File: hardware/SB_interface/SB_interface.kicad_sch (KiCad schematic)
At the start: 7 parts, among them J1 8P8C, J2 8P8C, J3 8P8C, K1 J104D2C12VDC.36S, Q1 2N7002

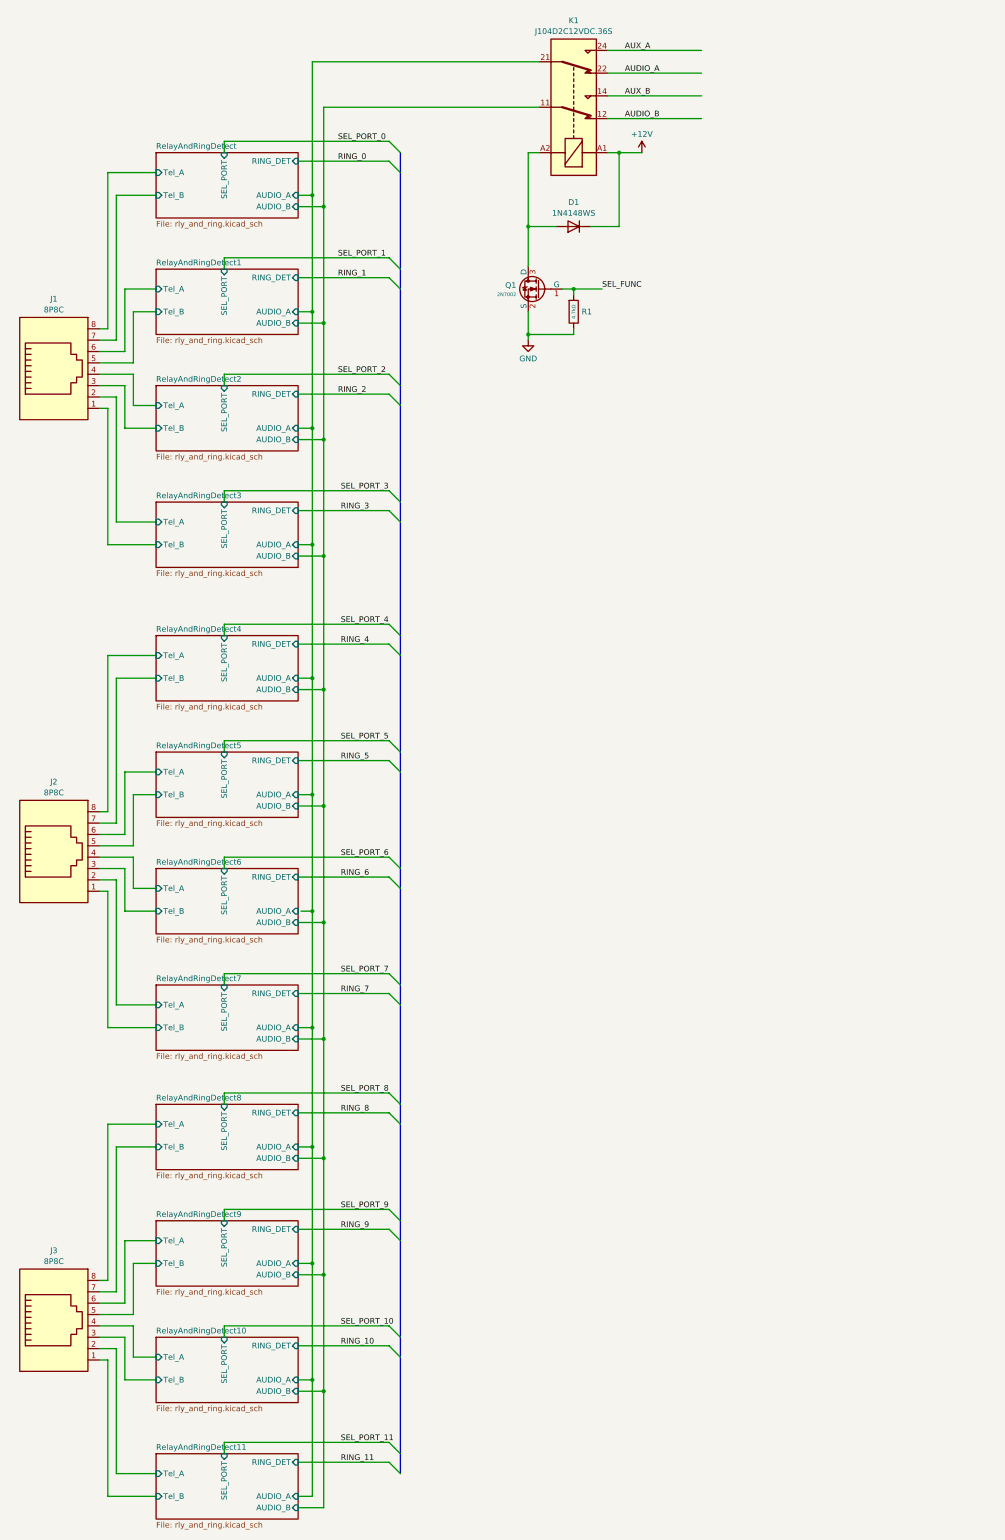
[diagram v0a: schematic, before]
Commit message: current source for ring det. + main 8p8c pinout corrected
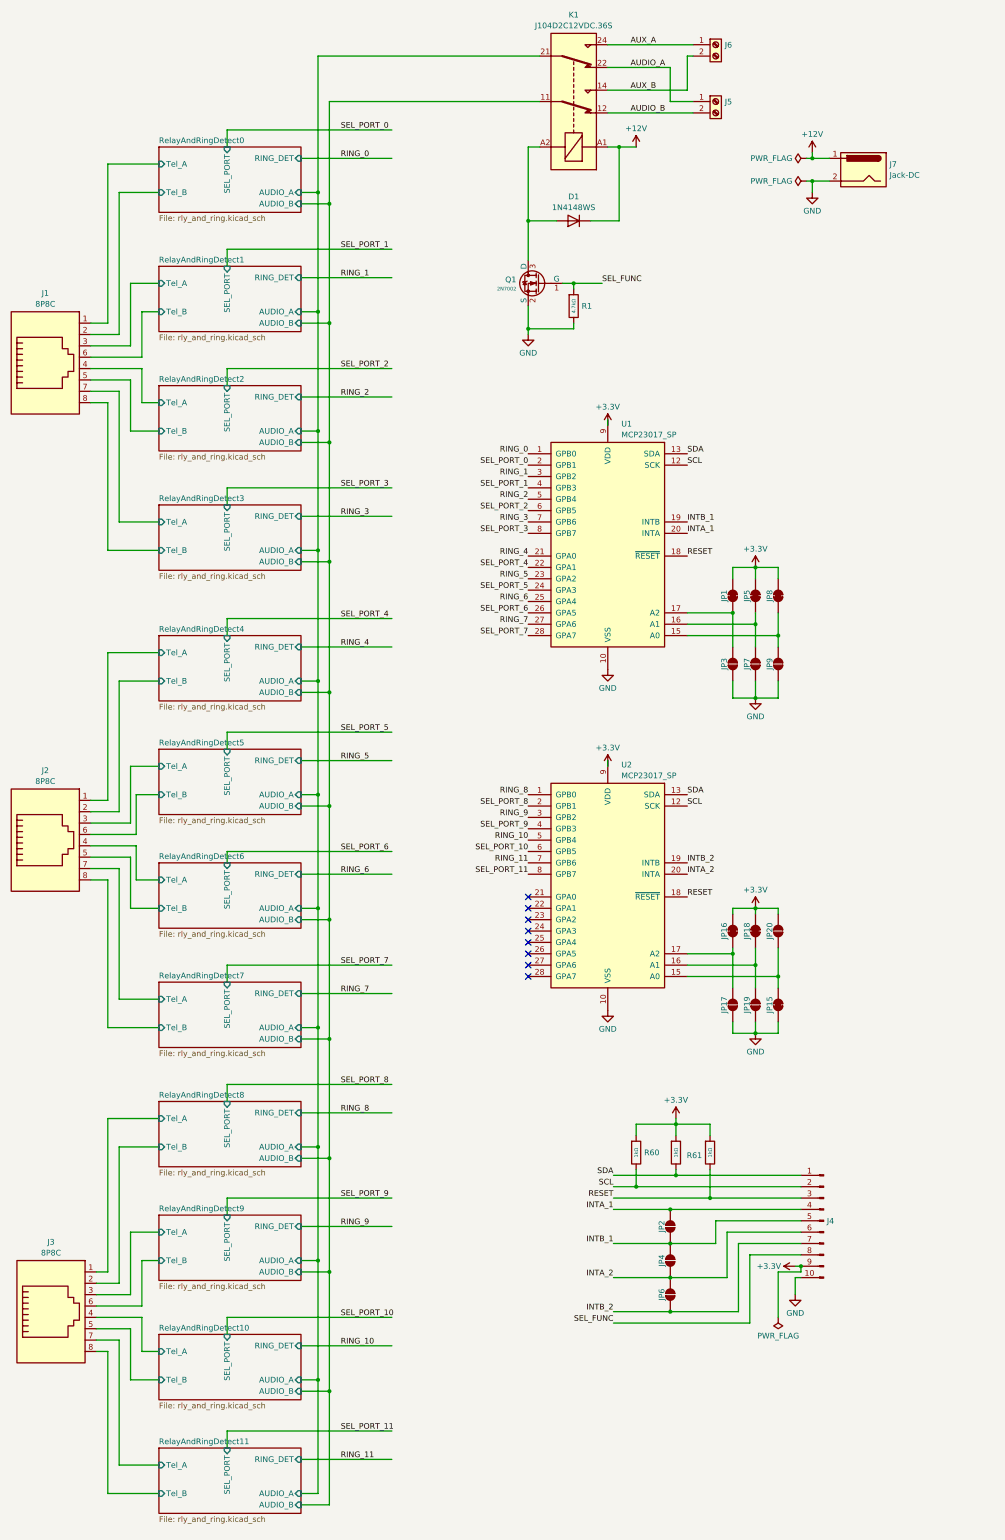
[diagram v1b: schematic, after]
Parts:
- added J4: Conn_01x10_Pin, symbol Connector:Conn_01x10_Pin
- added J5, J6: Screw_Terminal_01x02, symbol Connector:Screw_Terminal_01x02
- added J7: Jack-DC, symbol Connector:Jack-DC
- added JP1, JP15, JP16, JP18, JP5, JP8: SolderJumper_2_Bridged, symbol Jumper:SolderJumper_2_Bridged
- added JP17, JP19, JP2, JP20, JP3, JP4, JP6, JP7, JP9: SolderJumper_2_Open, symbol Jumper:SolderJumper_2_Open
- added R60, R61, R62: 1kΩ, PCM_JLCPCB:R_0805, symbol PCM_JLCPCB-Resistors:0805,1kΩ
- added U1, U2: MCP23017_SP, Package_DIP:DIP-28_W7.62mm, symbol Interface_Expansion:MCP23017_SP
- J1, J2, J3: symbol Connector:8P8C -> sb_interface:8P8C_TelPairs
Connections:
- net RelayAndRingDetect/Tel_A is gone; now on net RelayAndRingDetect3/Tel_B: J1.8
- net RelayAndRingDetect/Tel_B is gone; now on net RelayAndRingDetect3/Tel_A: J1.7
- net +12V: now also J7.1
- net AUDIO_A: now also J5.1 (Pin_1)
- net AUDIO_B: now also J5.2 (Pin_2)
- net AUX_A: now also J6.1 (Pin_1)
- net AUX_B: now also J6.2 (Pin_2)
- net GND: now also J4.10 (Pin_10), J7.2, JP15.2 (B), JP17.1 (A), JP19.1 (A), JP3.1 (A), JP7.1 (A), JP9.1 (A), U1.10 (VSS), U2.10 (VSS)
- net RING_0: now also U1.1 (GPB0)
- net RING_1: now also U1.3 (GPB2)
- net RING_10: now also U2.5 (GPB4)
- net RING_11: now also U2.7 (GPB6)
- net RING_2: now also U1.5 (GPB4)
- net RING_3: now also U1.7 (GPB6)
- net RING_4: now also U1.21 (GPA0)
- net RING_5: now also U1.23 (GPA2)
- net RING_6: now also U1.25 (GPA4)
- net RING_7: now also U1.27 (GPA6)
- net RING_8: now also U2.1 (GPB0)
- net RING_9: now also U2.3 (GPB2)
- net RelayAndRingDetect1/Tel_A: now also J1.3; no longer J1.6
- net RelayAndRingDetect1/Tel_B: now also J1.6; no longer J1.5
- net RelayAndRingDetect10/Tel_B: now also J3.5; no longer J3.3
- net RelayAndRingDetect11/Tel_A: now also J3.7; no longer J3.2
- net RelayAndRingDetect11/Tel_B: now also J3.8; no longer J3.1
- net RelayAndRingDetect2/Tel_B: now also J1.5; no longer J1.3
- net RelayAndRingDetect3/Tel_A: no longer J1.2
- net RelayAndRingDetect3/Tel_B: no longer J1.1
- net RelayAndRingDetect4/Tel_A: now also J2.1; no longer J2.8
- net RelayAndRingDetect4/Tel_B: now also J2.2; no longer J2.7
- net RelayAndRingDetect5/Tel_A: now also J2.3; no longer J2.6
- net RelayAndRingDetect5/Tel_B: now also J2.6; no longer J2.5
- net RelayAndRingDetect6/Tel_B: now also J2.5; no longer J2.3
- net RelayAndRingDetect7/Tel_A: now also J2.7; no longer J2.2
- net RelayAndRingDetect7/Tel_B: now also J2.8; no longer J2.1
- net RelayAndRingDetect8/Tel_A: now also J3.1; no longer J3.8
- net RelayAndRingDetect8/Tel_B: now also J3.2; no longer J3.7
- net RelayAndRingDetect9/Tel_A: now also J3.3; no longer J3.6
- net RelayAndRingDetect9/Tel_B: now also J3.6; no longer J3.5
- net SEL_FUNC: now also J4.8 (Pin_8)
- net SEL_PORT_0: now also U1.2 (GPB1)
- net SEL_PORT_1: now also U1.4 (GPB3)
- net SEL_PORT_10: now also U2.6 (GPB5)
- net SEL_PORT_11: now also U2.8 (GPB7)
- net SEL_PORT_2: now also U1.6 (GPB5)
- net SEL_PORT_3: now also U1.8 (GPB7)
- net SEL_PORT_4: now also U1.22 (GPA1)
- net SEL_PORT_5: now also U1.24 (GPA3)
- net SEL_PORT_6: now also U1.26 (GPA5)
- net SEL_PORT_7: now also U1.28 (GPA7)
- net SEL_PORT_8: now also U2.2 (GPB1)
- net SEL_PORT_9: now also U2.4 (GPB3)
- net RelayAndRingDetect/AUDIO_A renamed RelayAndRingDetect0/AUDIO_A
- net RelayAndRingDetect/AUDIO_B renamed RelayAndRingDetect0/AUDIO_B
- new net: JP16.2 (B), JP17.2 (B), U2.17 (A2)
- new net: JP15.1 (A), JP20.1 (A), U2.15 (A0)
- new net: JP1.2 (B), JP3.2 (B), U1.17 (A2)
- new net: JP18.2 (B), JP19.2 (B), U2.16 (A1)
- new net: JP5.2 (B), JP7.2 (B), U1.16 (A1)
- new net: JP8.2 (B), JP9.2 (B), U1.15 (A0)
- new net +3.3V: J4.9 (Pin_9), JP1.1 (A), JP16.1 (A), JP18.1 (A), JP20.2 (B), JP5.1 (A), JP8.1 (A), R60.1, R61.1, R62.1, U1.9 (VDD), U2.9 (VDD)
- new net INTA_1: J4.4 (Pin_4), JP2.2 (B), U1.20 (INTA)
- new net INTA_2: J4.6 (Pin_6), JP4.1 (A), JP6.2 (B), U2.20 (INTA)
- new net INTB_1: J4.5 (Pin_5), JP2.1 (A), JP4.2 (B), U1.19 (INTB)
- new net INTB_2: J4.7 (Pin_7), JP6.1 (A), U2.19 (INTB)
- new net RESET: J4.3 (Pin_3), R62.2, U1.18 (~{RESET}), U2.18 (~{RESET})
- new net RelayAndRingDetect0/Tel_A: J1.1
- new net RelayAndRingDetect0/Tel_B: J1.2
- new net SCL: J4.2 (Pin_2), R60.2, U1.12 (SCK), U2.12 (SCK)
- new net SDA: J4.1 (Pin_1), R61.2, U1.13 (SDA), U2.13 (SDA)
- no-connect marks 0 -> 8
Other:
- removed sheet RelayAndRingDetect
- added sheet RelayAndRingDetect0 (rly_and_ring.kicad_sch)
- moved on the sheet: D1, J1, J2, J3, K1, Q1, R1

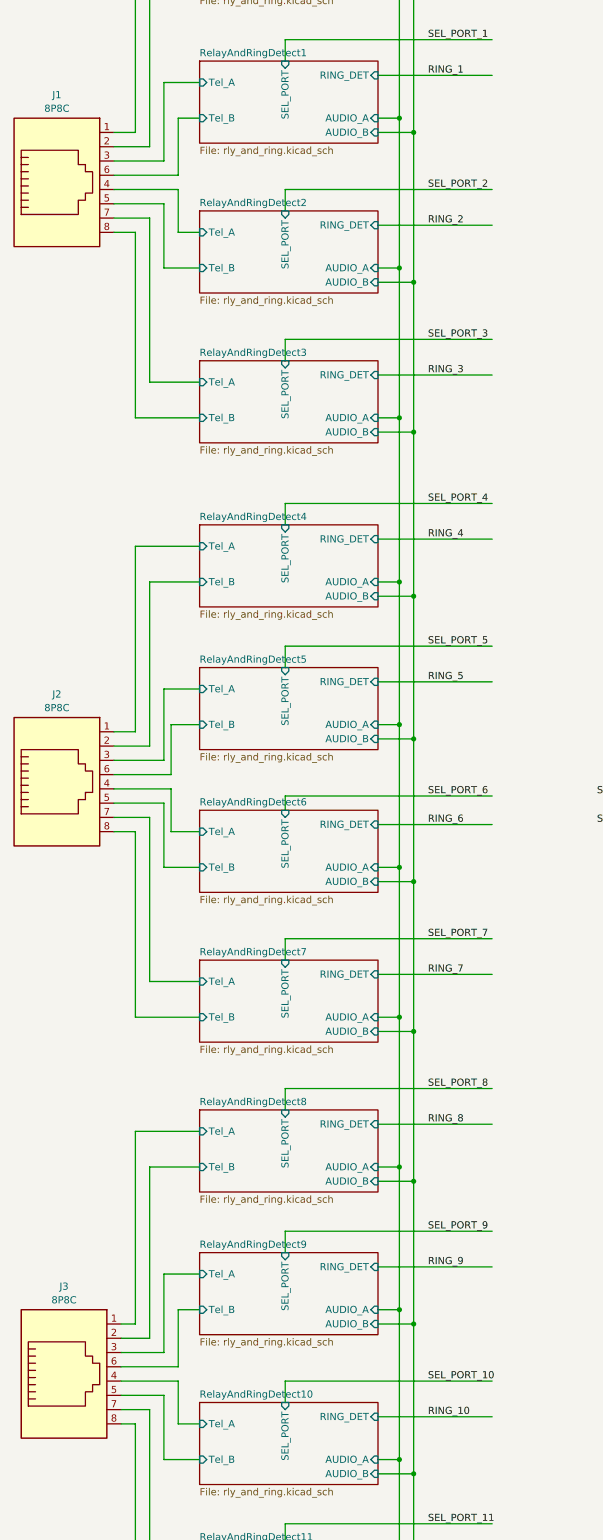
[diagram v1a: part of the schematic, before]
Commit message: assigneld footprints + started layout
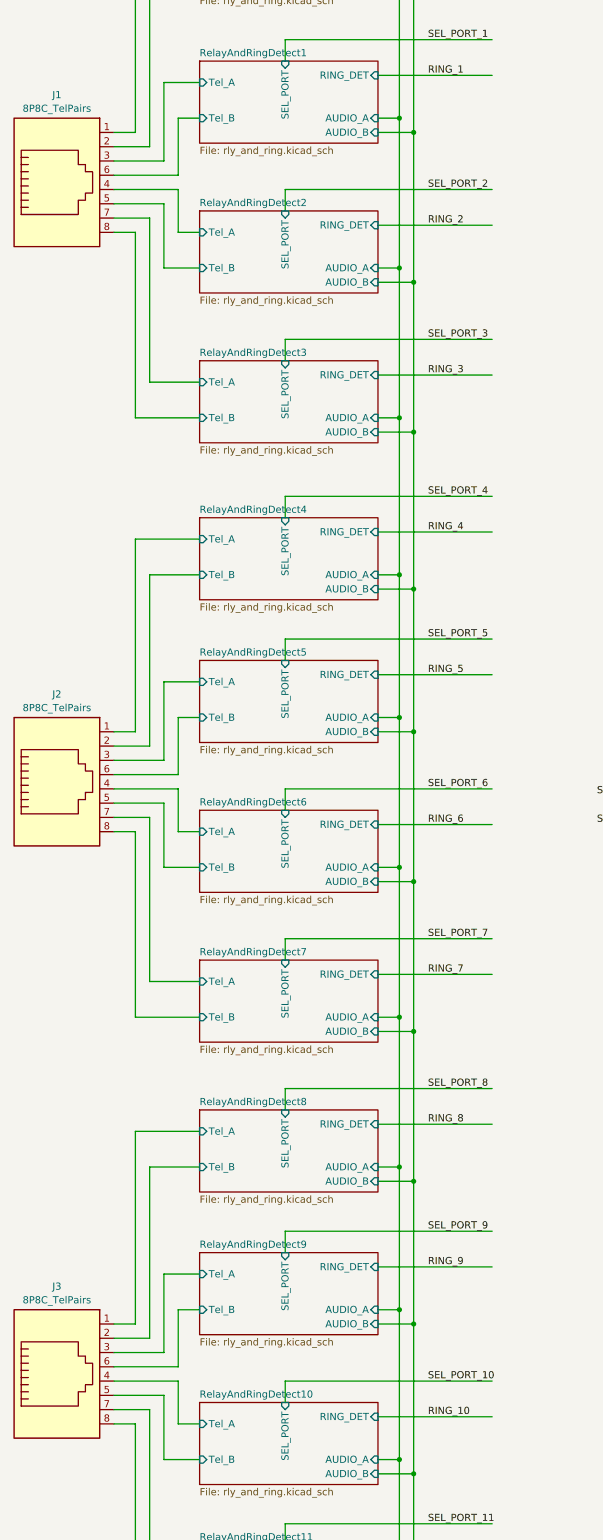
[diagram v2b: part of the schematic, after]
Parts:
- J1, J2, J3: value 8P8C -> 8P8C_TelPairs; footprint (none) -> Connector_RJ:RJ45_Amphenol_54602-x08_Horizontal; URL (none) -> https://www.digikey.at/de/products/detail/amphenol-cs-fci/5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; URLalt (none) -> https://www.neuhold-elektronik.at/steckverbindungen/modular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
- J4: footprint (none) -> Connector_PinHeader_2.54mm:PinHeader_1x10_P2.54mm_Vertical
- J5, J6: footprint (none) -> TerminalBlock_Phoenix:TerminalBlock_Phoenix_PT-1,5-2-3.5-H_1x02_P3.50mm_Horizontal; URL (none) -> https://www.digikey.at/de/products/detail/phoenix-contact/1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
- J7: footprint (none) -> Connector_BarrelJack:BarrelJack_Horizontal
- JP1, JP15, JP16, JP18, JP5, JP8: footprint (none) -> Jumper:SolderJumper-2_P1.3mm_Bridged_Pad1.0x1.5mm
- JP17, JP19, JP2, JP20, JP3, JP4, JP6, JP7, JP9: footprint (none) -> Jumper:SolderJumper-2_P1.3mm_Open_Pad1.0x1.5mm
- K1: footprint (none) -> sb_interface:J104D2C12VDC.36S

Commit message: replicated layout + added JLCPCB Design rules file
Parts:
- removed JP1, JP15, JP16, JP18, JP5, JP8: SolderJumper_2_Bridged, Jumper:SolderJumper-2_P1.3mm_Bridged_Pad1.0x1.5mm, symbol Jumper:SolderJumper_2_Bridged
- removed JP17, JP19, JP20, JP3, JP7, JP9: SolderJumper_2_Open, Jumper:SolderJumper-2_P1.3mm_Open_Pad1.0x1.5mm, symbol Jumper:SolderJumper_2_Open
- added C1, C2: 100nF, PCM_JLCPCB:C_0805, symbol PCM_JLCPCB-Capacitors:0805,100nF,(2)
- added JP10, JP11, JP12, JP13, JP14, JP15, JP4, JP5, JP6, JP7, JP8, JP9: Jumper_2_Small_Open, Connector_PinHeader_2.54mm:PinHeader_1x02_P2.54mm_Vertical, symbol Jumper:Jumper_2_Small_Open
- Q1: Stock 572214 -> 926097
- R1: Stock 2133514 -> 2078920
- R2: renamed from R60; Stock 10696298 -> 10624563
- R3: renamed from R61; Stock 10696298 -> 10624563
- R4: renamed from R62; Stock 10696298 -> 10624563
- renumbered J6 to J4, J4 to J6, JP2 to JP1, JP4 to JP2, JP6 to JP3
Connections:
- net +3.3V: now also C1.1, C2.1, JP10.2 (B), JP12.2 (B), JP14.2 (B), JP4.2 (B), JP6.2 (B), JP8.2 (B)
- net GND: now also C1.2, C2.2, JP11.1 (A), JP13.1 (A), JP15.1 (A), JP5.1 (A), JP7.1 (A), JP9.1 (A)
- net at U2.17 (A2): now also JP6.1 (A), JP7.2 (B)
- net at U2.15 (A0): now also JP14.1 (A), JP15.2 (B)
- net at U1.17 (A2): now also JP4.1 (A), JP5.2 (B)
- net at U2.16 (A1): now also JP10.1 (A), JP11.2 (B)
- net at U1.16 (A1): now also JP8.1 (A), JP9.2 (B)
- net at U1.15 (A0): now also JP12.1 (A), JP13.2 (B)
